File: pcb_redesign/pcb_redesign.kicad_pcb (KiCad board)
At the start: 4 copper layers, 48 x 31 mm, 23 parts, among them IC1 SPX1117M3-L-3-3_TR, J2 USB_B, U1 ESP32-S3-WROOM-1

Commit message: finished design
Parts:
- removed J2: USB_B, micro_usb_type_b:AMPHENOL_10118192-0002LF
- added J1: USB_B_Micro, micro_usb_type_b:AMPHENOL_10118192-0002LF, F.Cu at (149.9, 72.5)
- JP2: renamed from Motor R
- JP3: renamed from Motor L
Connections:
- R3 pad 1: VCC_3V3 -> 3.7_UNREG
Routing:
- net GND: track 31.6 -> 23.7 mm, vias 8 -> 9
- net 3.7_UNREG: track 34.1 -> 35.7 mm
- net VCC_3V3: track 34.0 -> 32.4 mm, vias 6 -> 5
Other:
- outline, holes or cut-outs redrawn
- board text added: "METR4810 Team 7"

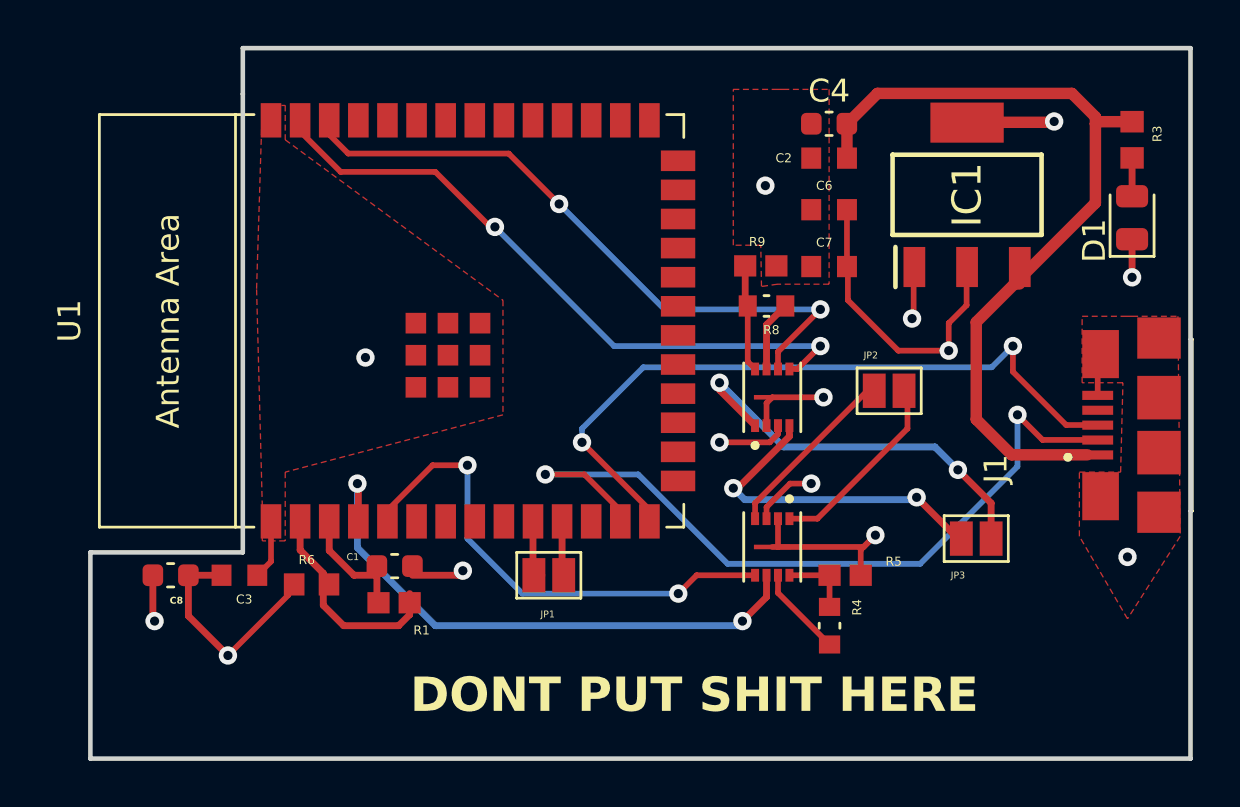
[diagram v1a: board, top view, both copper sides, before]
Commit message: finished adding decoupling caps, shipped off to jlc
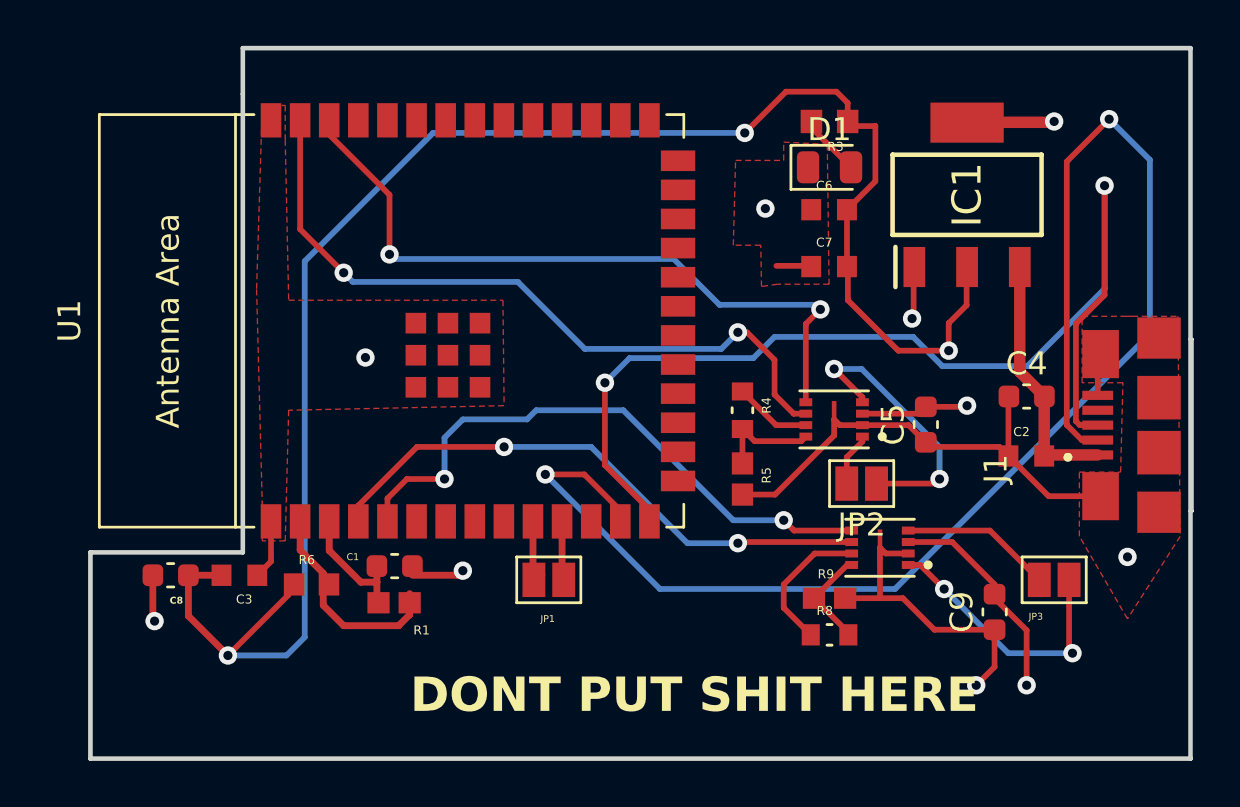
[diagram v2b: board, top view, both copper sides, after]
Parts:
- added C5: 10uF, Capacitor_SMD:C_0603_1608Metric, F.Cu at (142.4, 72.4)
- added C9: 10uF, Capacitor_SMD:C_0603_1608Metric, F.Cu at (145.4, 80.6)
- added G***: LOGO, bomba:bomb, B.Cu at (133.4, 74.5)
- R4, R8: value 30k -> 10k
- R5, R9: value 10k -> 30k
- moved C2 15.6 mm to (146.8, 73.8)
- moved R9 14.8 mm to (138.2, 80.0)
- moved C4 14.7 mm to (146.8, 71.2)
- moved R8 14.6 mm to (138.2, 81.6), turned to 0 degrees
- moved D1 13.4 mm to (138.2, 61.2), turned to 0 degrees
- moved R3 13.2 mm to (138.2, 59.2), turned to 180 degrees
- moved R4 10.1 mm to (134.4, 71.8), turned to -90 degrees
- moved A3908EEETR-T3 8.07 mm to (140.4, 77.8), turned to 180 degrees
- moved A3908EEETR-T1 6.19 mm to (138.4, 72.2), turned to 180 degrees
- moved R5 6.14 mm to (134.4, 74.8), turned to -90 degrees
- moved JP2 4.22 mm to (139.7, 75.0), turned to 180 degrees
- moved JP3 3.85 mm to (148.1, 79.2)
- moved JP1 0.20 mm to (126.0, 79.2)
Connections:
- A3908EEETR-T1 pad 5: ENA Right Motor -> ENB Left Motor
- A3908EEETR-T1 pad 6: ENB Right Motor -> ENA Left Motor
- A3908EEETR-T3 pad 5: ENA Left Motor -> ENA Right Motor
- A3908EEETR-T3 pad 6: ENB Left Motor -> ENB Right Motor
- R3 pad 1: 3.7_UNREG -> VCC_3V3
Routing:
- net VCC_3V3: track 32.4 -> 93.8 mm, vias 5 -> 6
- net D-: track 34.1 -> 62.8 mm
- net 3.7_UNREG: track 35.7 -> 11.0 mm
- net GND: track 23.7 -> 46.8 mm, vias 9 -> 7
- net D+: track 30.5 -> 46.8 mm
- net Net-(A3908EEETR-T3-OUTA): track 14.8 -> 6.61 mm, vias 2 -> 0
- net Net-(A3908EEETR-T1-OUTB): track 8.49 -> 2.33 mm
- net Net-(A3908EEETR-T3-OUTB): track 18.1 -> 12.0 mm
- net Net-(A3908EEETR-T1-OUTA): track 7.91 -> 12.2 mm, vias 0 -> 2
- net ENA Right Motor: track 21.9 -> 26.1 mm
- net Net-(A3908EEETR-T3-VREF): track 3.09 -> 6.21 mm
- net ENA Left Motor: track 28.8 -> 31.6 mm
- net ENB Left Motor: track 28.6 -> 31.0 mm
- net Net-(A3908EEETR-T1-VSET): track 3.13 -> 4.57 mm
- net Net-(D1-A): track 1.67 -> 2.52 mm
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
